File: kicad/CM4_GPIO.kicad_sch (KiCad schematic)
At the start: 38 parts

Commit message: Add files via upload
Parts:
- renumbered U to C3, U to C35, U to C36, U to C37, U to C38, U to C39, U to C40, U to D3, U to D4, U to D5, U to FB1, U to FB2, U to J12, U to J13, U to J14, U to J15, U to J16, U to J17, U to J18, U to J19, U to Module1, U to R20, U to R21, U to R22, U to R23, U to R24, U to R25, U to R26, U to R27, U to R28, U to R29, U to R30, U to R31, U to R32, U to U10, U to U11, U to U8, U to U9
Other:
- note removed: "A button bwteen pins 13-14 can be used to wake up compute module from power down"
- note removed: "If compute modules is awake RUN_PG will be high so the button doesn't do anything If the compute module is asleep then RUN_PG will be at 0v and so pull global enable low"

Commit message: Fixing remaining errors
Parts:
- renumbered U10 to U, U8 to U, U11 to U, Module1 to U, J17 to U, C40 to U, D3 to U, R20 to U, D4 to U, R23 to U, J14 to U, R30 to U, R31 to U, J16 to U, J13 to U, C38 to U, R26 to U, C39 to U, R21 to U, C36 to U, R22 to U, FB1 to U, FB2 to U, C3 to U, C35 to U, C37 to U, R28 to U, J19 to U, J15 to U, U9 to U, J12 to U, R32 to U, R29 to U, J18 to U, R25 to U, R27 to U, R24 to U, D5 to U

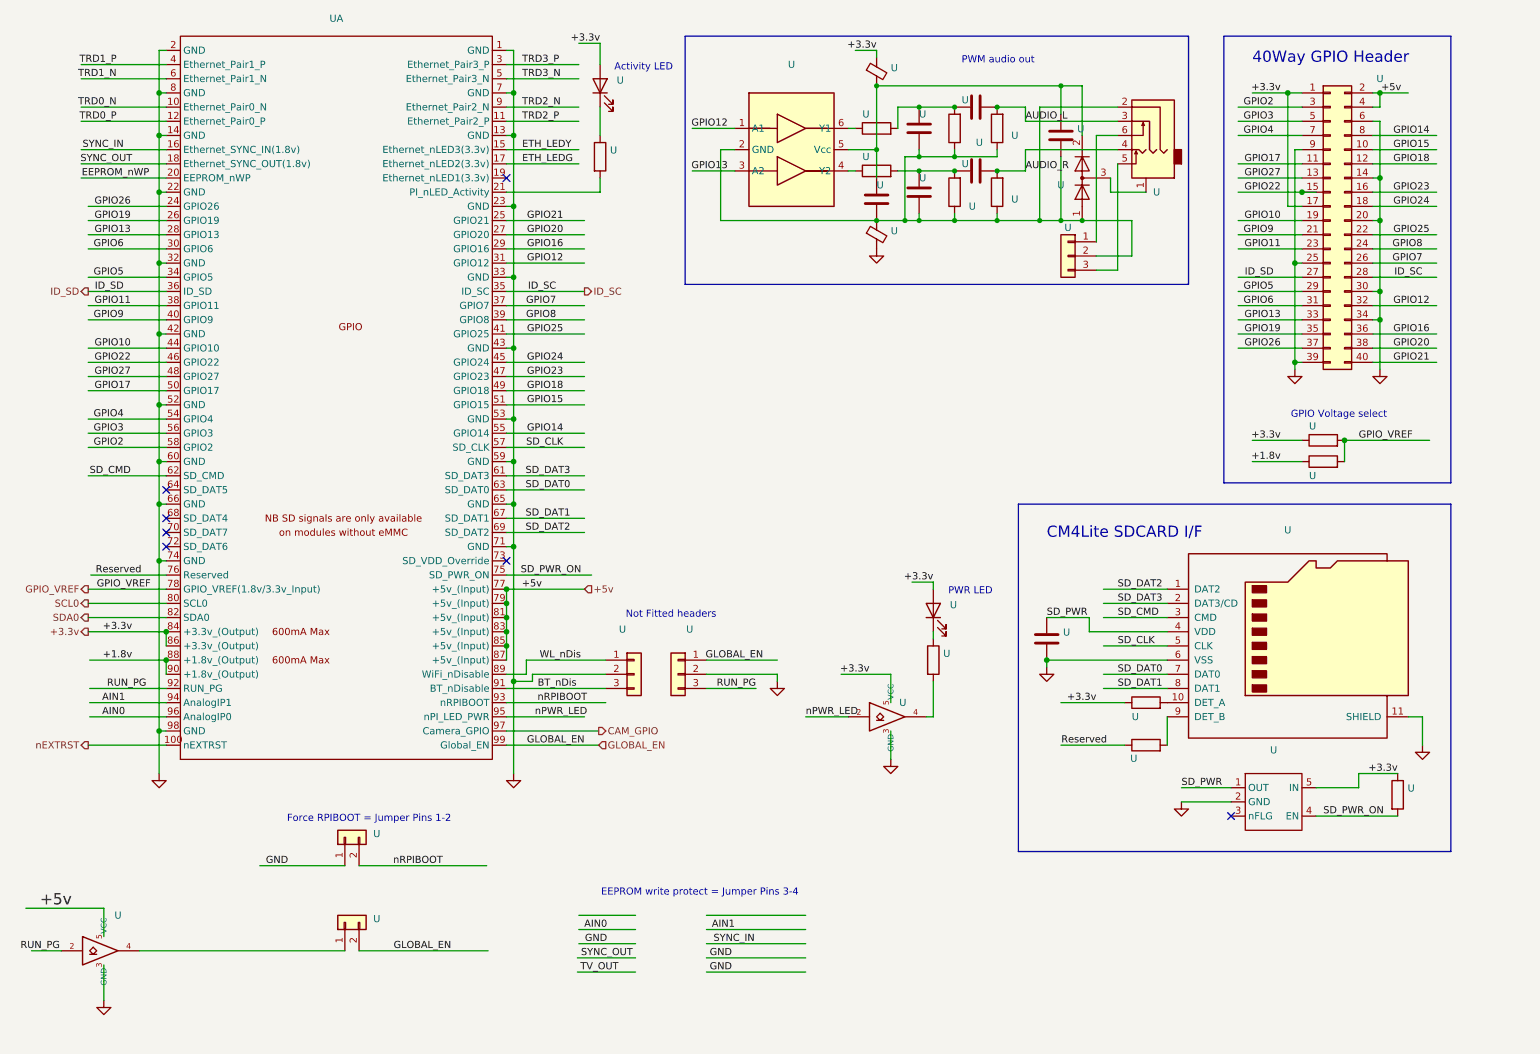
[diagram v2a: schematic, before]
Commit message: Mirroring CAM, DSI, new GPDI pinout fix #2 #3 #5 #12
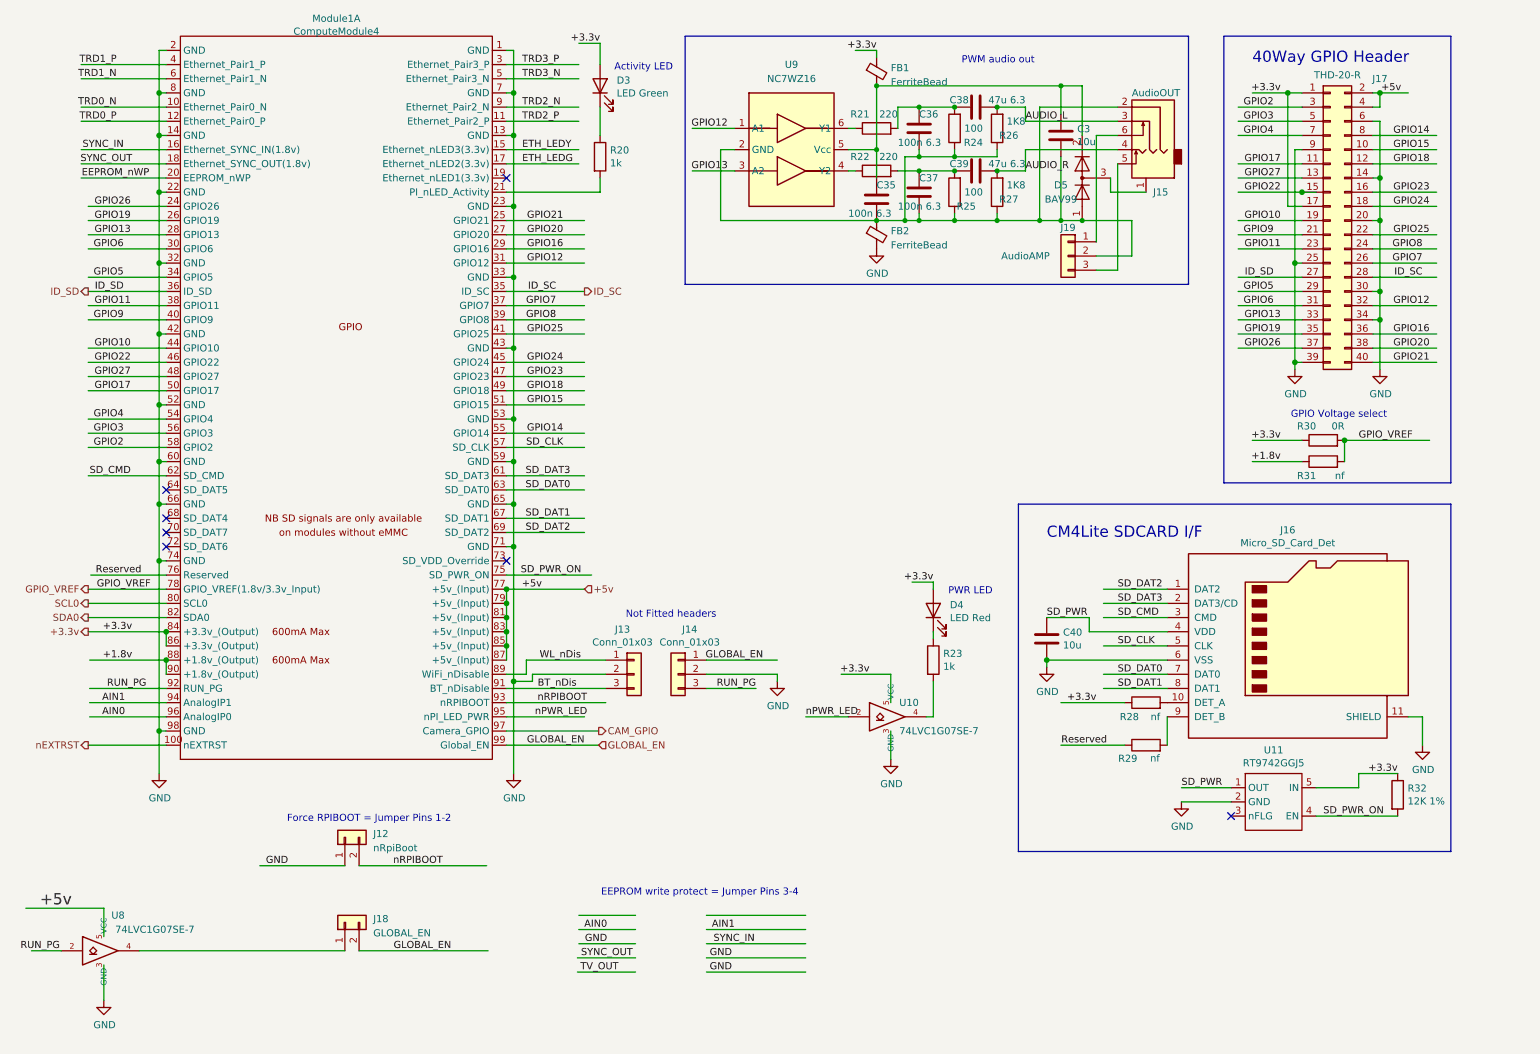
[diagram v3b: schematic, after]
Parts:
- C3, C40: renamed from U; value (none) -> 10u; footprint (none) -> Capacitor_SMD:C_0805_2012Metric
- C35, C36, C37: renamed from U; value (none) -> 100n 6.3; footprint (none) -> Capacitor_SMD:C_0402_1005Metric
- C38, C39: renamed from U; value (none) -> 47u 6.3; footprint (none) -> Capacitor_SMD:C_0805_2012Metric
- D3: renamed from U; value (none) -> LED Green; footprint (none) -> LED_SMD:LED_0603_1608Metric
- D4: renamed from U; value (none) -> LED Red; footprint (none) -> LED_SMD:LED_0603_1608Metric
- D5: renamed from U; value (none) -> BAV99; footprint (none) -> Package_TO_SOT_SMD:SOT-23
- FB1, FB2: renamed from U; value (none) -> FerriteBead; footprint (none) -> Inductor_SMD:L_0805_2012Metric
- J12: renamed from U; value (none) -> nRpiBoot; footprint (none) -> Connector_PinHeader_1.00mm:PinHeader_1x02_P1.00mm_Vertical
- J13, J14: renamed from U; value (none) -> Conn_01x03; footprint (none) -> Connector_PinHeader_2.54mm:PinHeader_1x03_P2.54mm_Vertical
- J15: renamed from U; value (none) -> AudioOUT; footprint (none) -> Connector_Audio:Jack_3.5mm_PJ311_Horizontal
- J16: renamed from U; value (none) -> Micro_SD_Card_Det; footprint (none) -> CM4IO:SDCARD_MOLEX_503398-1892
- J17: renamed from U; value (none) -> THD-20-R; footprint (none) -> Connector_PinHeader_2.54mm:PinHeader_2x20_P2.54mm_Vertical
- J18: renamed from U; value (none) -> GLOBAL_EN; footprint (none) -> Connector_PinHeader_1.00mm:PinHeader_1x02_P1.00mm_Vertical
- J19: renamed from U; value (none) -> AudioAMP; footprint (none) -> Connector_PinHeader_2.00mm:PinHeader_1x04_P2.00mm_Horizontal
- Module1: renamed from U; value (none) -> ComputeModule4; footprint (none) -> CM4IO:Raspberry-Pi-4-Compute-Module-noholes
- R20, R23: renamed from U; value (none) -> 1k; footprint (none) -> Resistor_SMD:R_0402_1005Metric
- R21, R22: renamed from U; value (none) -> 220; footprint (none) -> Resistor_SMD:R_0402_1005Metric
- R24, R25: renamed from U; value (none) -> 100; footprint (none) -> Resistor_SMD:R_0402_1005Metric
- R26, R27: renamed from U; value (none) -> 1K8; footprint (none) -> Resistor_SMD:R_0402_1005Metric
- R28, R29: renamed from U; value (none) -> nf; footprint (none) -> Resistor_SMD:R_0402_1005Metric
- R30: renamed from U; value (none) -> 0R; footprint (none) -> Resistor_SMD:R_0805_2012Metric_Pad1.20x1.40mm_HandSolder
- R31: renamed from U; value (none) -> nf; footprint (none) -> Resistor_SMD:R_0805_2012Metric_Pad1.20x1.40mm_HandSolder
- R32: renamed from U; value (none) -> 12K 1%; footprint (none) -> Resistor_SMD:R_0402_1005Metric
- U10, U8: renamed from U; value (none) -> 74LVC1G07SE-7; footprint (none) -> Package_TO_SOT_SMD:SOT-353_SC-70-5
- U11: renamed from U; value (none) -> RT9742GGJ5; footprint (none) -> Package_TO_SOT_SMD:SOT-23-5
- U9: renamed from U; value (none) -> NC7WZ16; footprint (none) -> CM4IO:SC-88-6_2x2.1mm

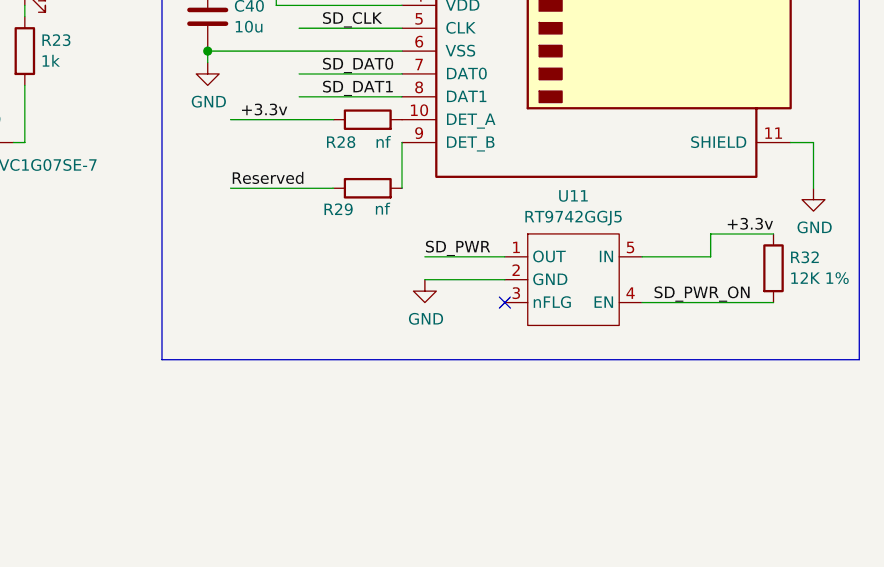
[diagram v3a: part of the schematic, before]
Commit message: Adding I2C poullups to schematics
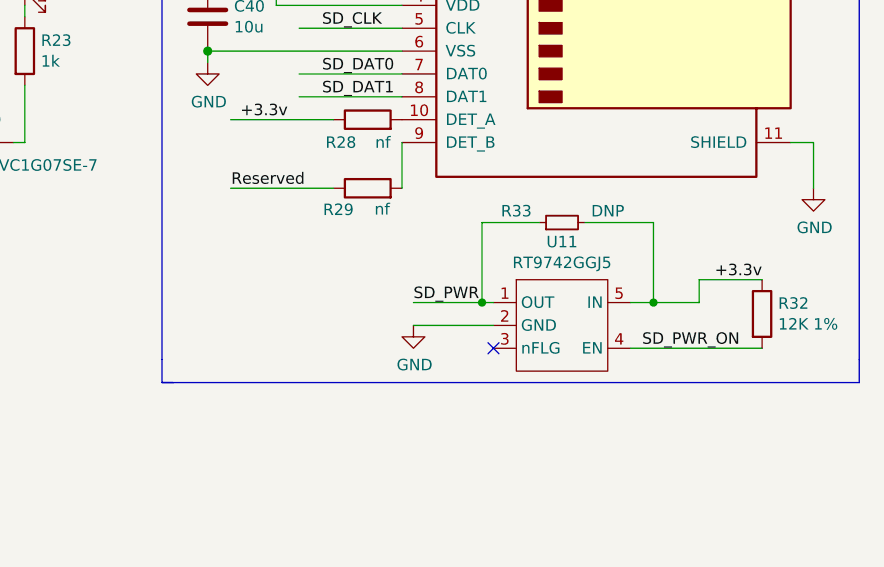
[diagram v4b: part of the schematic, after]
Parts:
- added R33: DNP, symbol Device:R_Small
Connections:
- net +3.3v: now also R33.2
- net SD_PWR: now also R33.1
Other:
- moved on the sheet: R32, U11

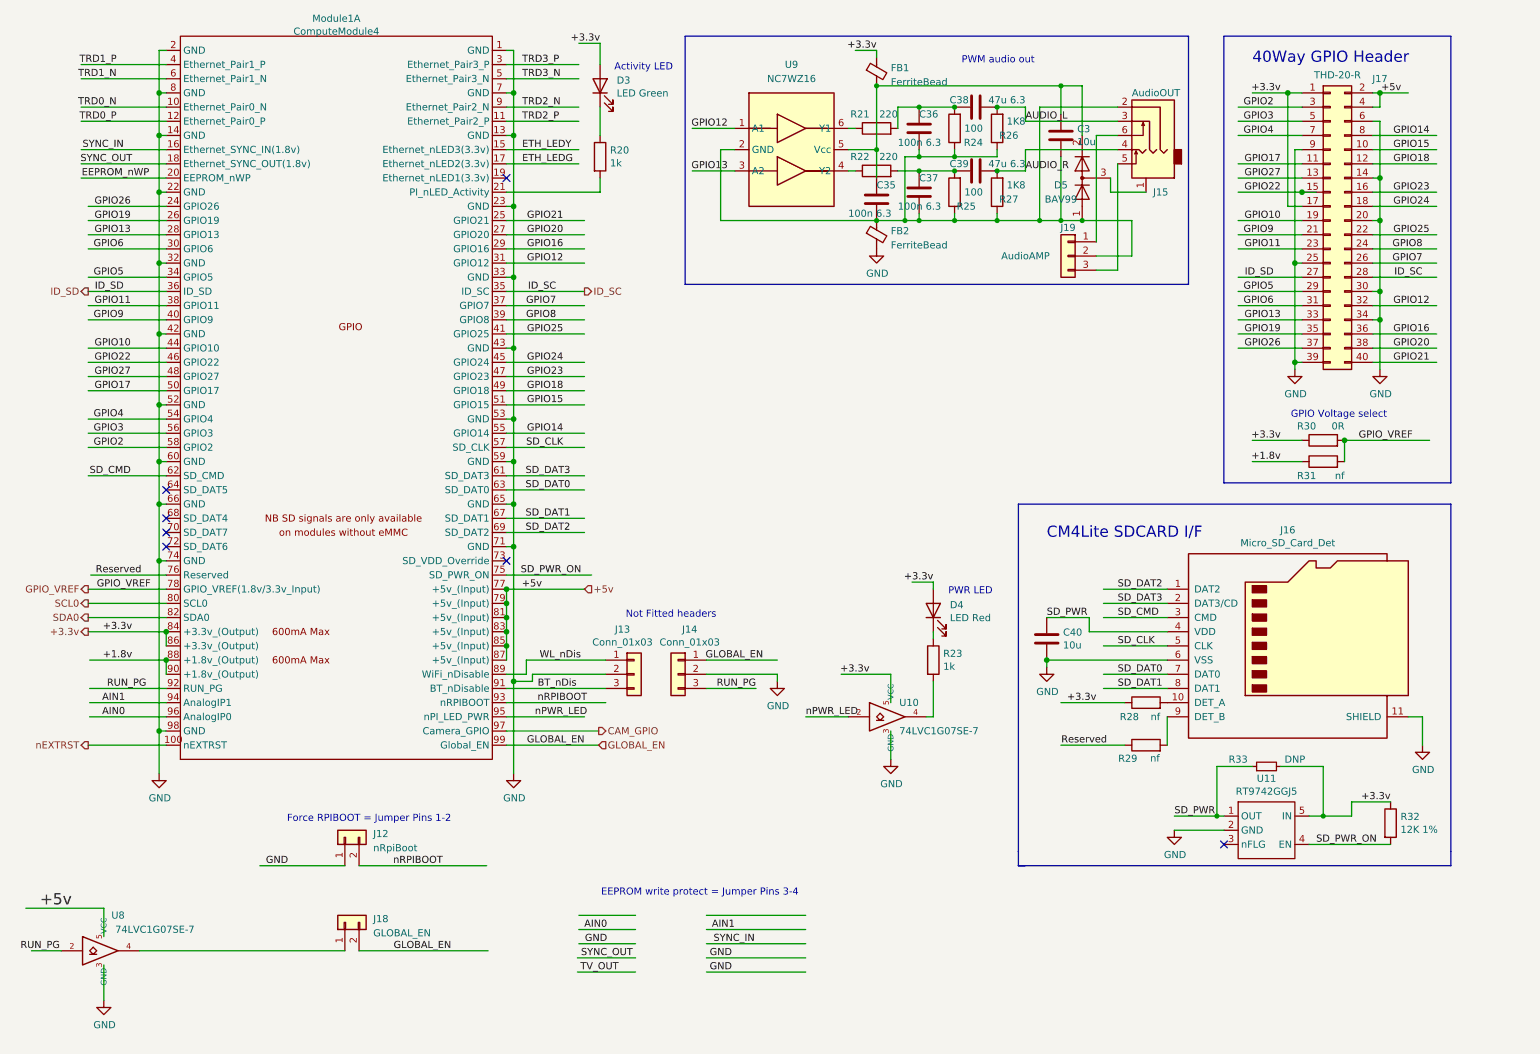
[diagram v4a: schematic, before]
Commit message: Adding ethernet connector to schematics
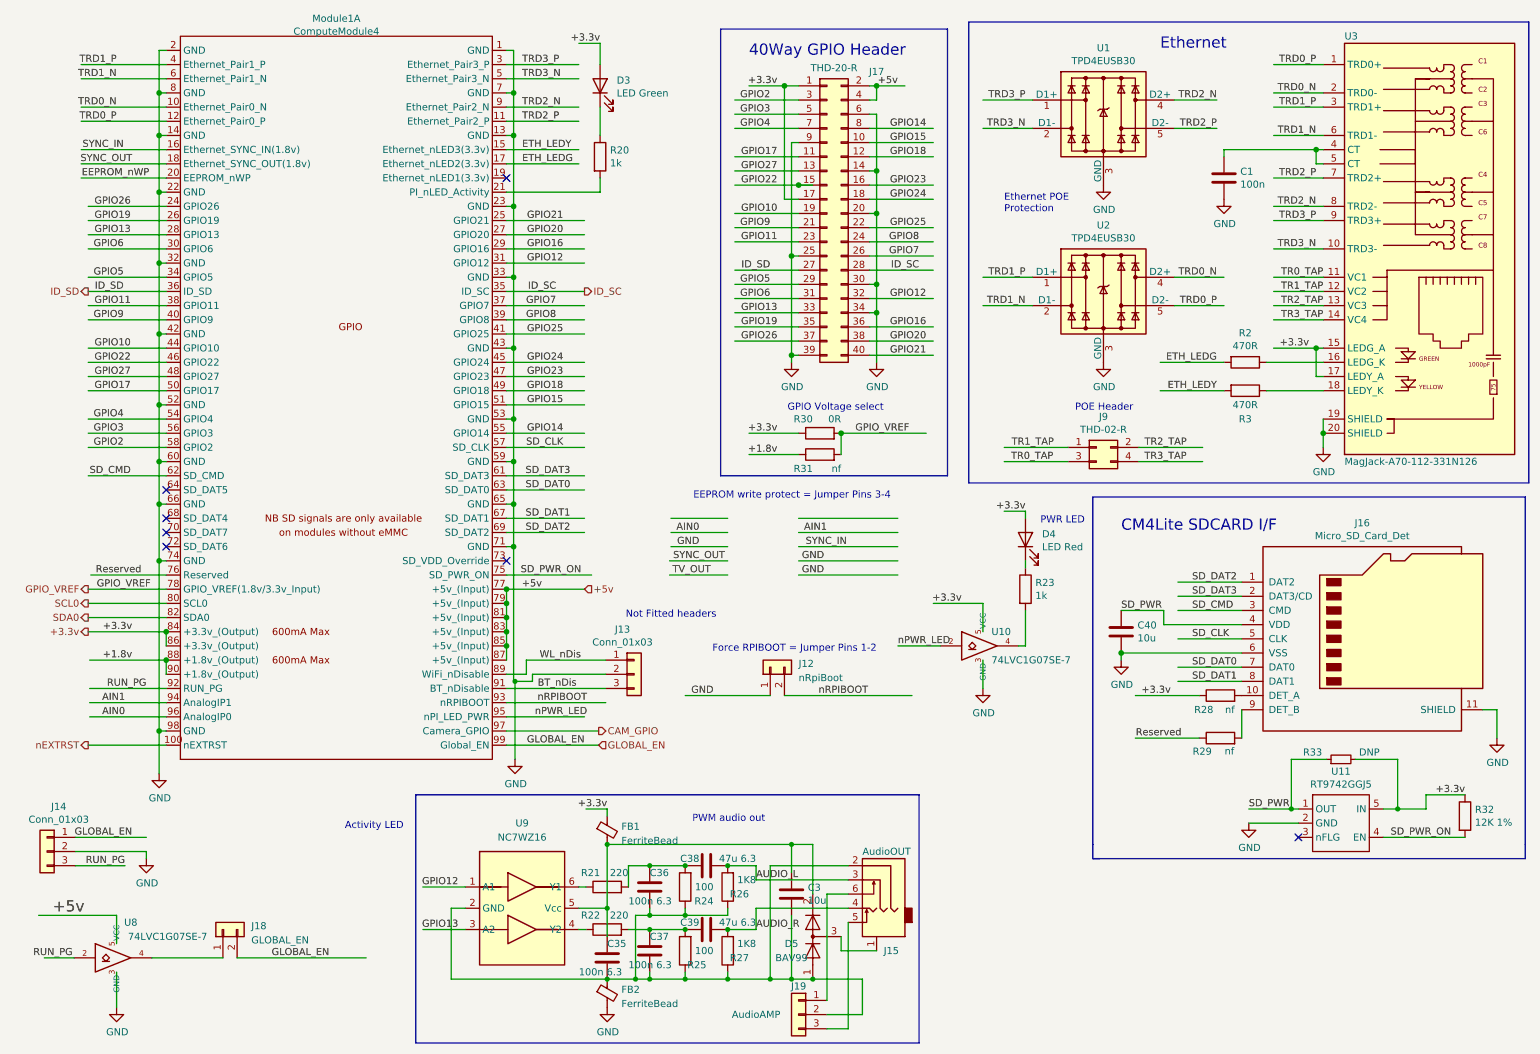
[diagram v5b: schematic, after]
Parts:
- added C1: 100n, Capacitor_SMD:C_0402_1005Metric, symbol Device:C
- added J9: THD-02-R, Connector_PinHeader_2.54mm:PinHeader_2x02_P2.54mm_Vertical, symbol Connector_Generic:Conn_02x02_Odd_Even
- added R2, R3: 470R, Resistor_SMD:R_0402_1005Metric, symbol Device:R
- added U1, U2: TPD4EUSB30, Package_SON:USON-10_2.5x1.0mm_P0.5mm, symbol CM4IO:TPD4EUSB30
- added U3: MagJack-A70-112-331N126, CM4IO:TRJG0926HENL, symbol CM4IO:MagJack-A70-112-331N126
- R33: footprint (none) -> Resistor_SMD:R_0402_1005Metric
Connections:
- net +3.3v: now also U3.15 (LEDG_A), U3.17 (LEDY_A)
- net ETH_LEDG: now also R2.2
- net ETH_LEDY: now also R3.2
- net GND: now also C1.2, U1.3 (GND), U1.8 (GND), U2.3 (GND), U2.8 (GND), U3.19 (SHIELD), U3.20 (SHIELD)
- net TRD0_N: now also U2.4 (D2+), U2.7, U3.2 (TRD0-)
- net TRD0_P: now also U2.5 (D2-), U2.6, U3.1 (TRD0+)
- net TRD1_N: now also U2.2 (D1-), U2.9, U3.6 (TRD1-)
- net TRD1_P: now also U2.1 (D1+), U2.10, U3.3 (TRD1+)
- net TRD2_N: now also U1.4 (D2+), U1.7, U3.8 (TRD2-)
- net TRD2_P: now also U1.5 (D2-), U1.6, U3.7 (TRD2+)
- net TRD3_N: now also U1.2 (D1-), U1.9, U3.10 (TRD3-)
- net TRD3_P: now also U1.1 (D1+), U1.10, U3.9 (TRD3+)
- new net: R3.1, U3.18 (LEDY_K)
- new net: R2.1, U3.16 (LEDG_K)
- new net: C1.1, U3.4 (CT), U3.5 (CT)
- new net TR0_TAP: J9.3 (Pin_3), U3.11 (VC1)
- new net TR1_TAP: J9.1 (Pin_1), U3.12 (VC2)
- new net TR2_TAP: J9.2 (Pin_2), U3.13 (VC3)
- new net TR3_TAP: J9.4 (Pin_4), U3.14 (VC4)
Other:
- note added: "Ethernet"
- note added: "Ethernet POE Protection"
- note added: "POE Header"
- moved on the sheet: C3, C35, C36, C37, C38, C39, C40, D4, D5, FB1, FB2, J12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
